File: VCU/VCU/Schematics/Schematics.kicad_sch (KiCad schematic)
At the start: 1 part, among them U1 ATSAMC21J18A-ANT

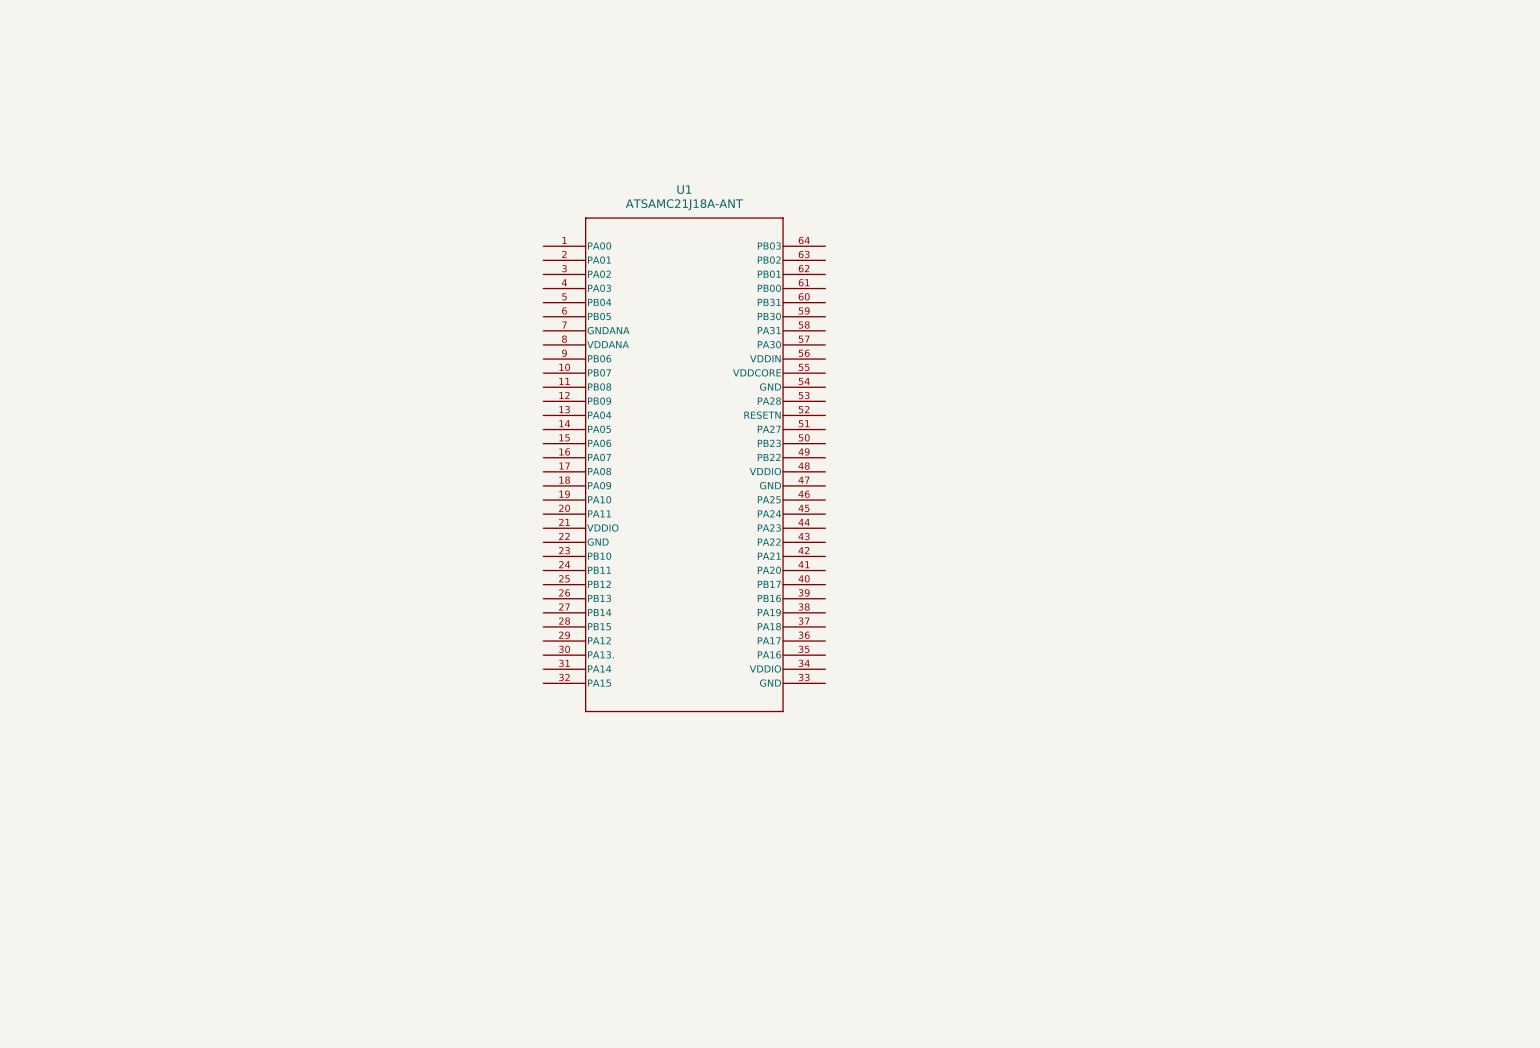
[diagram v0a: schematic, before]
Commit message: Update schematics
Ajout de la transmission CAN et du schéma d'alimentation du VCU
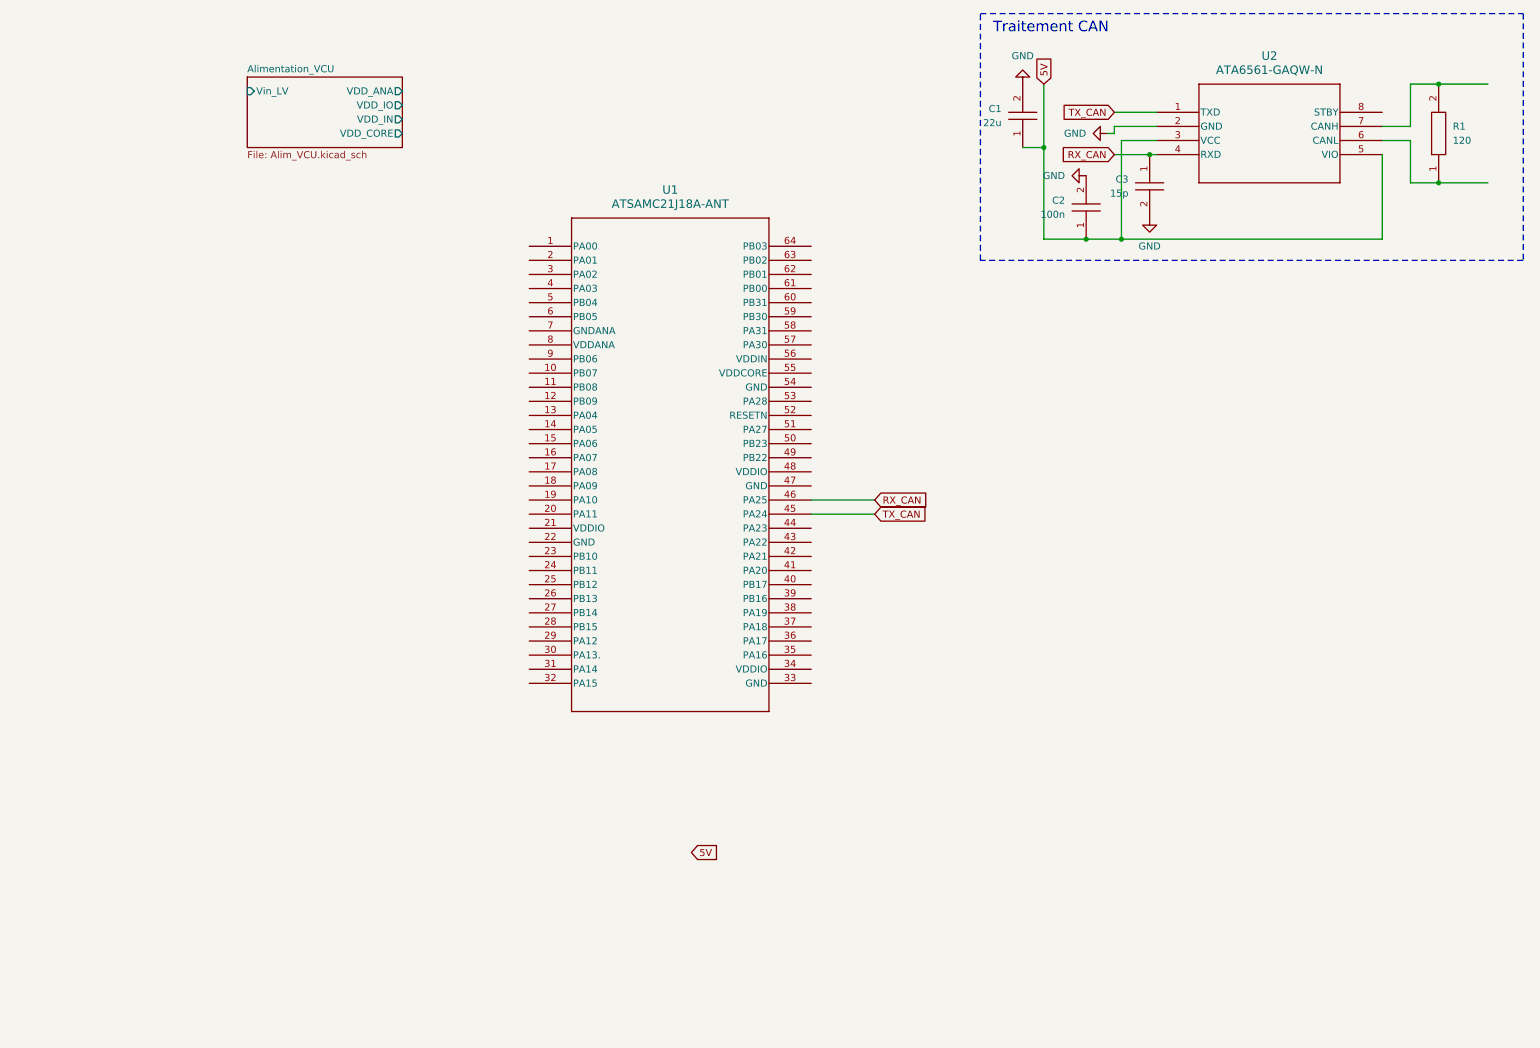
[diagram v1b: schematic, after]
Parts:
- added C1: 22u, EPSA_lib:CAPC2012X130N, symbol EPSA_lib:Condensateur 0805Y1000104JXT
- added C2: 100n, EPSA_lib:CAPC2012X130N, symbol EPSA_lib:Condensateur 0805Y1000104JXT
- added C3: 15p, EPSA_lib:CAPC2012X130N, symbol EPSA_lib:Condensateur 0805Y1000104JXT
- added R1: 120, EPSA_lib:RESC3216X70N, symbol EPSA_lib:Résistance RK73H2BLTDD2152F
- added U2: ATA6561-GAQW-N, SOIC8_4P9X3P9MC_MCH, symbol ATA6561-GAQW-N:ATA6561-GAQW-N
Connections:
- net TX_CAN: now reaches U1.45 (PA24)
- net TX_CAN: now also U2.1 (TXD)
- net RX_CAN: now reaches U1.46 (PA25)
- net RX_CAN: now also C3.1, U2.4 (RXD)
- new net: R1.1, U2.6 (CANL)
- new net: R1.2, U2.7 (CANH)
- new net 5V: C1.1, C2.1, U2.3 (VCC), U2.5 (VIO)
- new net GND: C1.2, C2.2, C3.2, U2.2 (GND)
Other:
- added sheet Alimentation_VCU (Alim_VCU.kicad_sch)
- note added: "Traitement CAN"
- moved on the sheet: U1

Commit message: Update schematics
Update du schema avec ajout des embases et wiring de l'alimentation
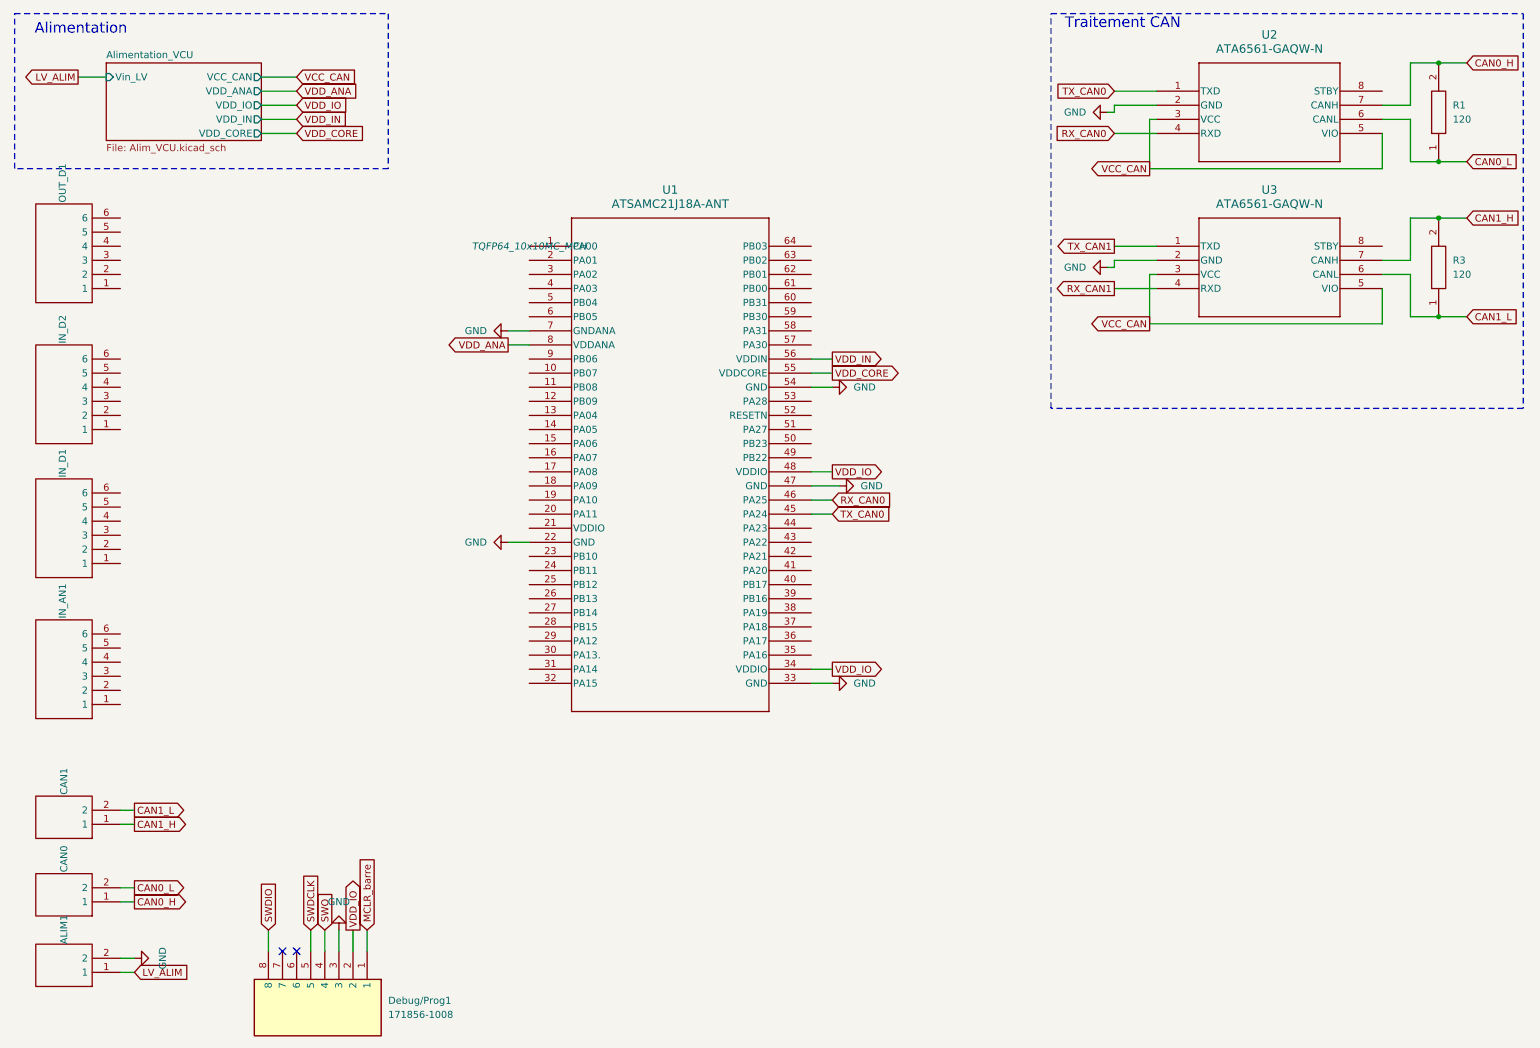
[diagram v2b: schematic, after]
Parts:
- removed C1: 22u, EPSA_lib:CAPC2012X130N, symbol EPSA_lib:Condensateur 0805Y1000104JXT
- removed C2: 100n, EPSA_lib:CAPC2012X130N, symbol EPSA_lib:Condensateur 0805Y1000104JXT
- removed C3: 15p, EPSA_lib:CAPC2012X130N, symbol EPSA_lib:Condensateur 0805Y1000104JXT
- added ALIM1, CAN0, CAN1: 2P Angle 171857-4002, EPSA_lib:1718574002, symbol EPSA_lib:2P Angle 171857-4002
- added Debug/Prog1: 171856-1008, SHDR8W99P0X254_1X8_2017X635X1124P, symbol 171856-1008:171856-1008
- added IN_AN1, IN_D1, IN_D2, OUT_D1: 6P Droit 22-11-2062, EPSA_lib:HDRV6W87P0X254_1X6_1509X635X1092P, symbol EPSA_lib:6P Droit 22-11-2062
- added R3: 120, EPSA_lib:RESC3216X70N, symbol EPSA_lib:Résistance RK73H2BLTDD2152F
- added U3: ATA6561-GAQW-N, SOIC8_4P9X3P9MC_MCH, symbol ATA6561-GAQW-N:ATA6561-GAQW-N
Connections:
- net GND: now also U1.22 (GND), U1.33 (GND), U1.47 (GND), U1.54 (GND), U1.7 (GNDANA), ALIM1.2, Debug/Prog1.3, U3.2 (GND)
- net VDD_IO: now reaches U1.34 (VDDIO)
- net VDD_IO: now also U1.48 (VDDIO), Debug/Prog1.2
- net VDD_CORE: now reaches U1.55 (VDDCORE)
- net VDD_IN: now reaches U1.56 (VDDIN)
- net VDD_ANA: now reaches U1.8 (VDDANA)
- net CAN0_L: now reaches R1.1, U2.6 (CANL)
- net CAN0_L: now also CAN0.2
- net CAN0_H: now reaches R1.2, U2.7 (CANH)
- net CAN0_H: now also CAN0.1
- net 5V renamed VCC_CAN
- net VCC_CAN: now also U3.3 (VCC), U3.5 (VIO)
- net RX_CAN renamed RX_CAN0
- net TX_CAN renamed TX_CAN0
- new net CAN1_H: CAN1.1, R3.2, U3.7 (CANH)
- new net CAN1_L: CAN1.2, R3.1, U3.6 (CANL)
- new net LV_ALIM: ALIM1.1
- new net MCLR_barre: Debug/Prog1.1
- new net RX_CAN1: U3.4 (RXD)
- new net SWDCLK: Debug/Prog1.5
- new net SWDIO: Debug/Prog1.8
- new net SWO: Debug/Prog1.4
- new net TX_CAN1: U3.1 (TXD)
- no-connect marks 0 -> 2
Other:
- sheet Alimentation_VCU ports: added VCC_CAN; removed none
- note added: "Alimentation"
- moved on the sheet: R1, U2

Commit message: Update schematics VCU et ajout protocoles de tests
Ajout de protocoles de tests et ajout de l'interface microSD dans les schematics
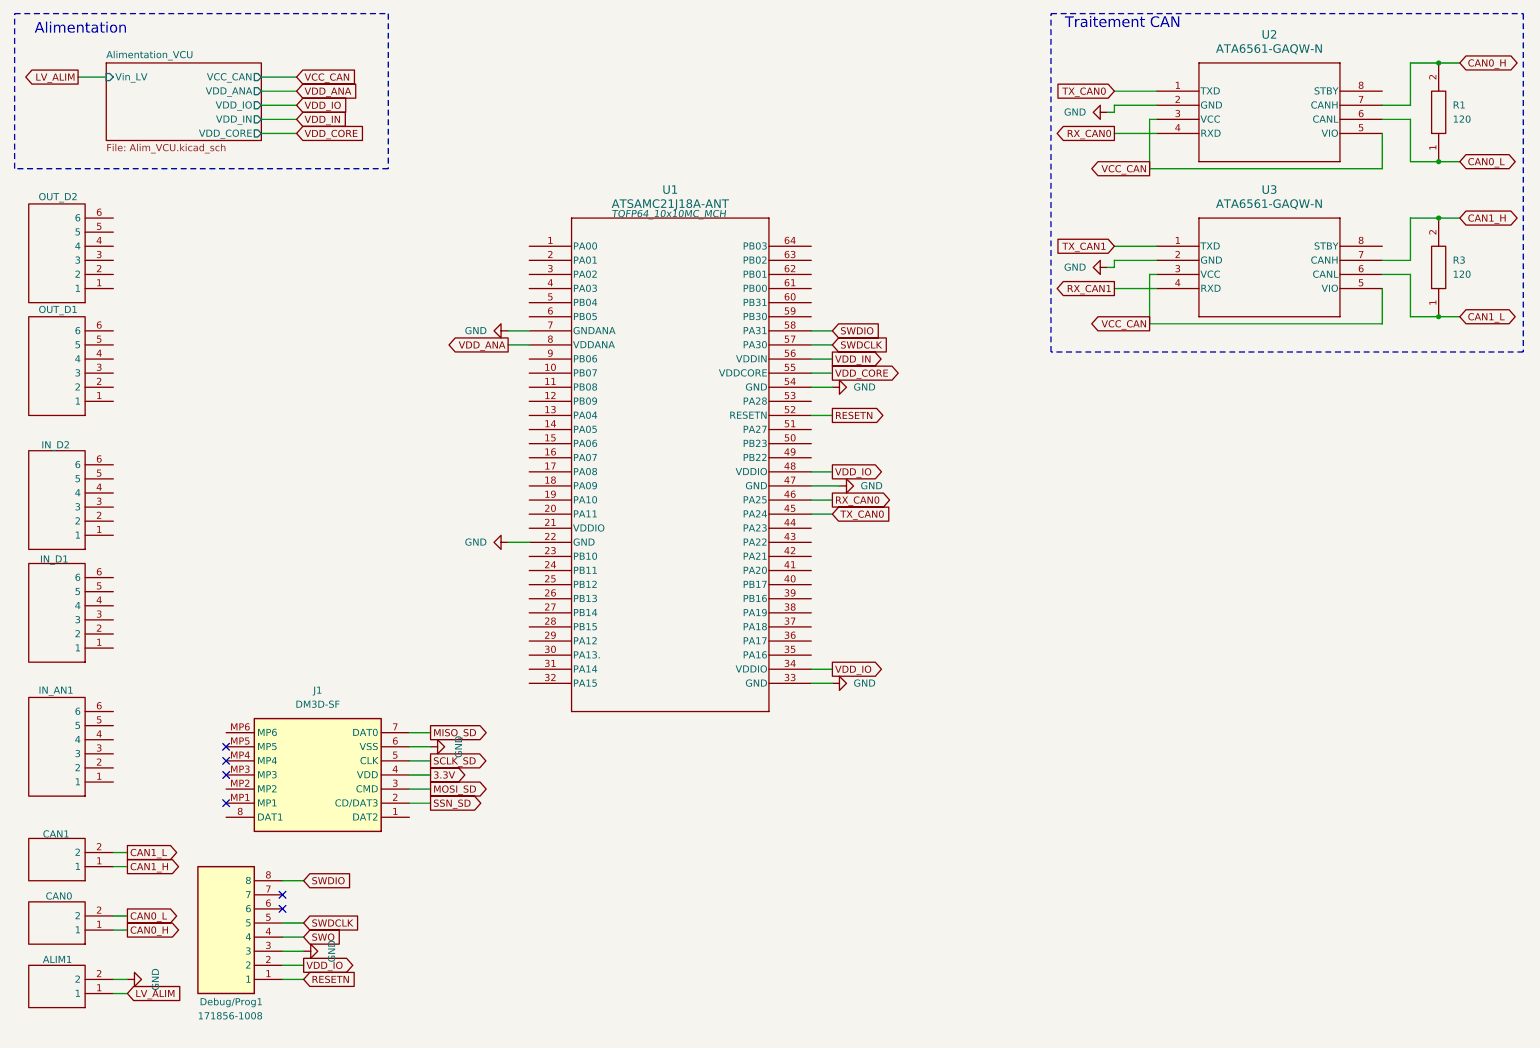
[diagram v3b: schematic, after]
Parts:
- added J1: DM3D-SF, DM3DSF, symbol DM3D-SF:DM3D-SF
- added OUT_D2: 6P Droit 22-11-2062, EPSA_lib:HDRV6W87P0X254_1X6_1509X635X1092P, symbol EPSA_lib:6P Droit 22-11-2062
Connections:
- net MCLR_barre is gone; now on net RESETN: Debug/Prog1.1
- net GND: now also J1.6 (VSS)
- net SWDCLK: now also U1.57 (PA30)
- net SWDIO: now also U1.58 (PA31)
- net RESETN: now reaches U1.52 (RESETN)
- new net 3.3V: J1.4 (VDD)
- new net MISO_SD: J1.7 (DAT0)
- new net MOSI_SD: J1.3 (CMD)
- new net SCLK_SD: J1.5 (CLK)
- new net SSN_SD: J1.2 (CD/DAT3)
- no-connect marks 2 -> 6
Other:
- moved on the sheet: ALIM1, CAN0, CAN1, Debug/Prog1, IN_AN1, IN_D1, IN_D2, OUT_D1

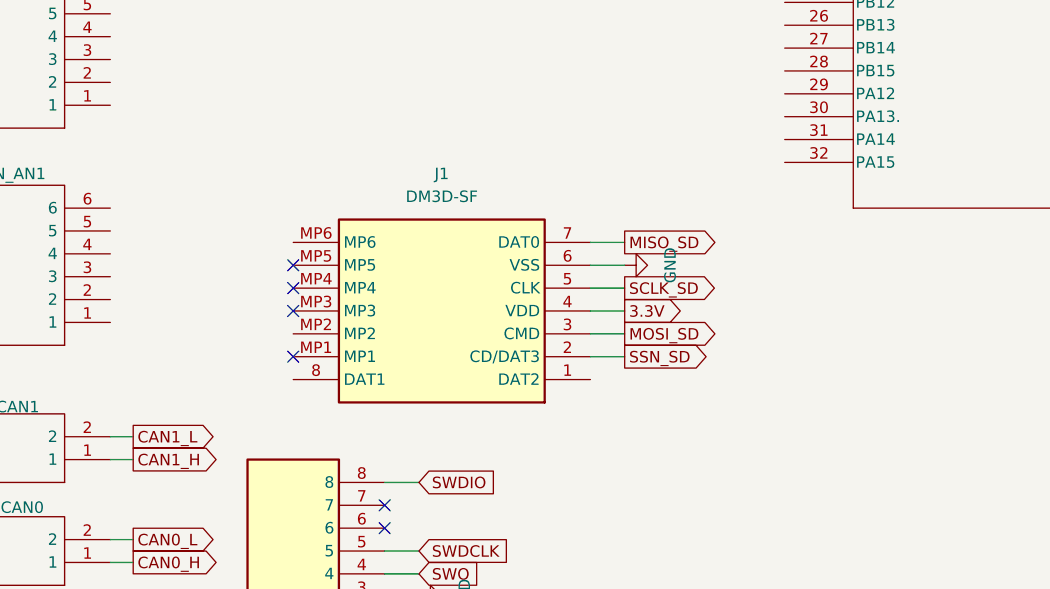
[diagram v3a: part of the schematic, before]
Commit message: Ajout readME et Update schematics
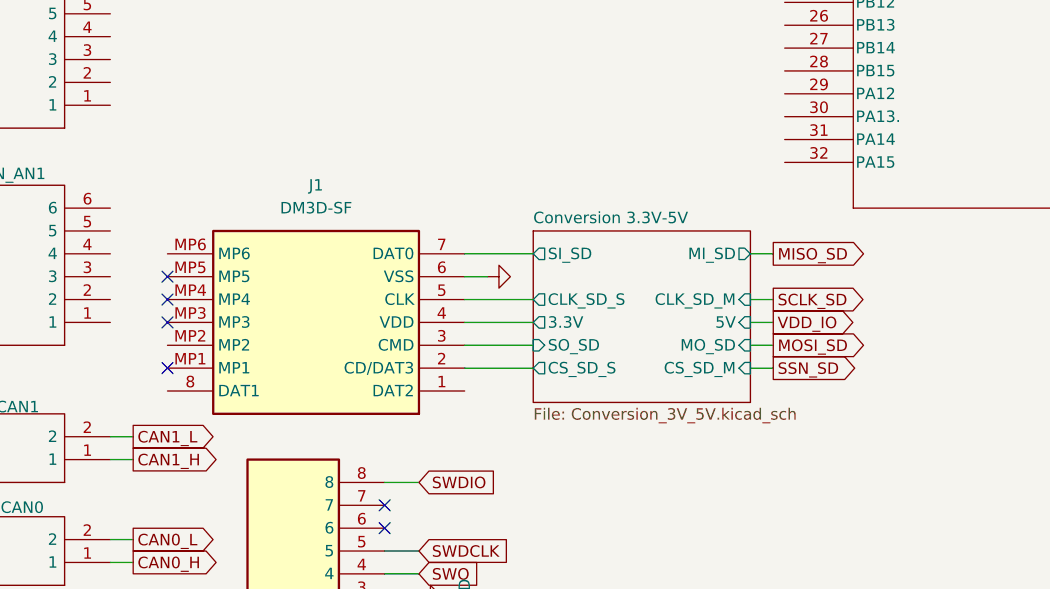
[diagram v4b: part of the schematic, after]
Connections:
- net MISO_SD: no longer J1.7 (DAT0)
- net MOSI_SD: no longer J1.3 (CMD)
- net SCLK_SD: no longer J1.5 (CLK)
- net SSN_SD: no longer J1.2 (CD/DAT3)
- net 3.3V renamed Conversion 3.3V-5V/3.3V
- new net Conversion 3.3V-5V/CLK_SD_S: J1.5 (CLK)
- new net Conversion 3.3V-5V/CS_SD_S: J1.2 (CD/DAT3)
- new net Conversion 3.3V-5V/SI_SD: J1.7 (DAT0)
- new net Conversion 3.3V-5V/SO_SD: J1.3 (CMD)
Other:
- added sheet Conversion 3.3V-5V (Conversion_3V_5V.kicad_sch)
- moved on the sheet: J1
